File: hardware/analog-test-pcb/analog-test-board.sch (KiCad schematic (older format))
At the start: 0 parts

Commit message: Typo.
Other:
- note added: "Requirement:\nThe input to the HX1 module needs a swing from 0 to 5V\nin order to achive the ±5kHz deviation (typical specs\nfrom the datasheet).\n\nProblem:\nThe output of the DS8500 is 500mVpp (typ) with a 1.5V\nof DC offset. The maximum load at the ouput is 30kOHM\n(by specs in the datasheet). This needs to be analogly\nprocessed in order to fit the signal level required by the\nHX1 module\n\n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"
- note removed: "Requirement:\nThe input to the HX1 module need a swing from 0 to 5V\nin order to achive the ±5kHz deviation (typical specs\nfrom the datasheet).\n\nProblem:\nThe output of the DS8500 is 500mVpp (typ) with a 1.5V\nof DC offset. The maximum load at the ouput is 30kOHM\n(by specs in the datasheet). This needs to be analogly\nprocessed in order to fit the signal level required by the\nHX1 module\n\nS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"
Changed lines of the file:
@@
 $EndDescr
 Text Notes 650  2000 0    60   ~ 12
-Requirement:\nThe input to the HX1 module need a swing from 0 to 5V\nin order to achive the ±5kHz deviation (typical specs\nfrom the datasheet).\n\nProblem:\nThe output of the DS8500 is 500mVpp (typ) with a 1.5V\nof DC offset. The maximum load at the ouput is 30kOHM\n(by specs in the datasheet). This needs to be analogly\nprocessed in order to fit the signal level required by the\nHX1 module\n\nSolution:\nDo some analog processing!
+Requirement:\nThe input to the HX1 module needs a swing from 0 to 5V\nin order to achive the ±5kHz deviation (typical specs\nfrom the datasheet).\n\nProblem:\nThe output of the DS8500 is 500mVpp (typ) with a 1.5V\nof DC offset. The maximum load at the ouput is 30kOHM\n(by specs in the datasheet). This needs to be analogly\nprocessed in order to fit the signal level required by the\nHX1 module\n\nSolution:\nDo some analog processing!
 $EndSCHEMATC

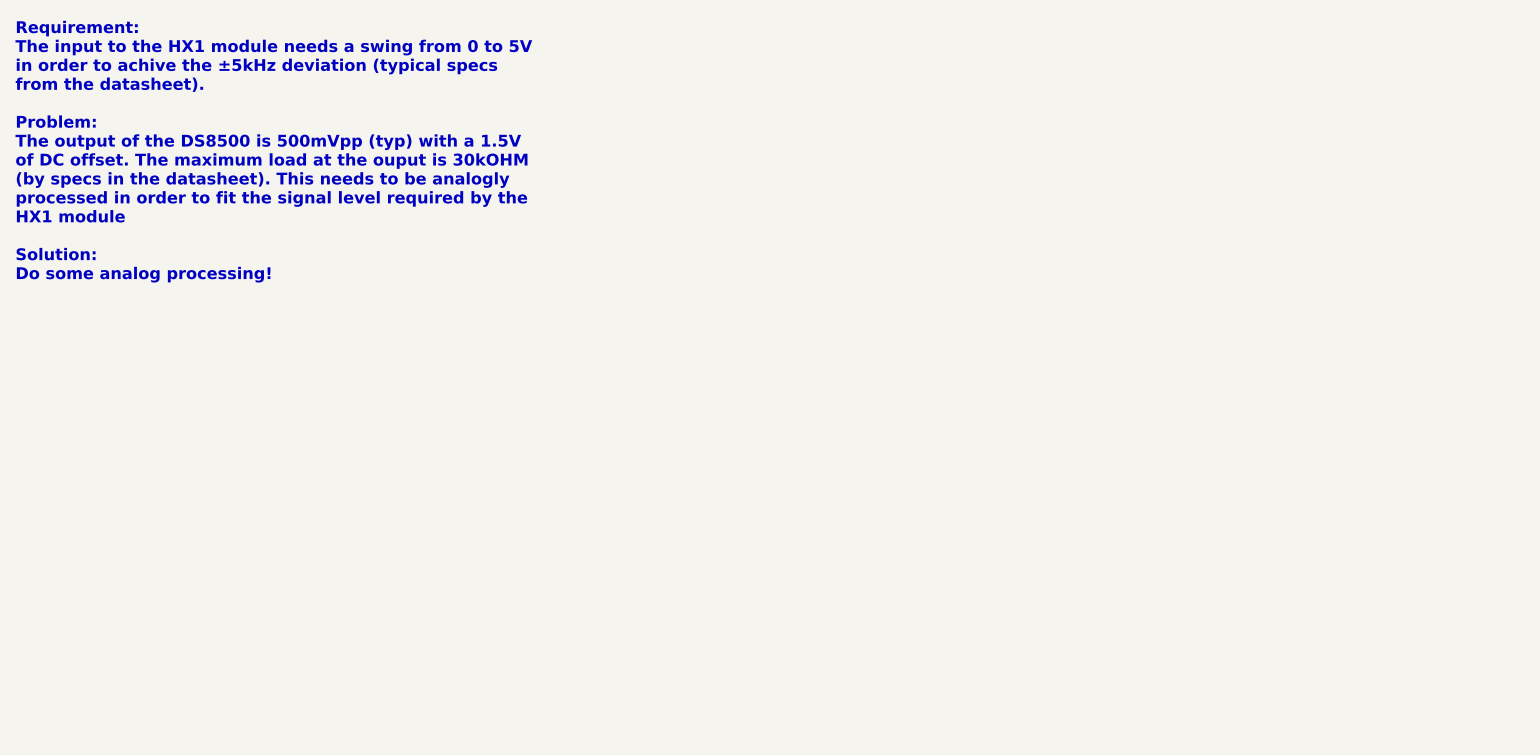
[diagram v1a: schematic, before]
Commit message: The schematic. A buffer followed by a inverting amp with a DC offset
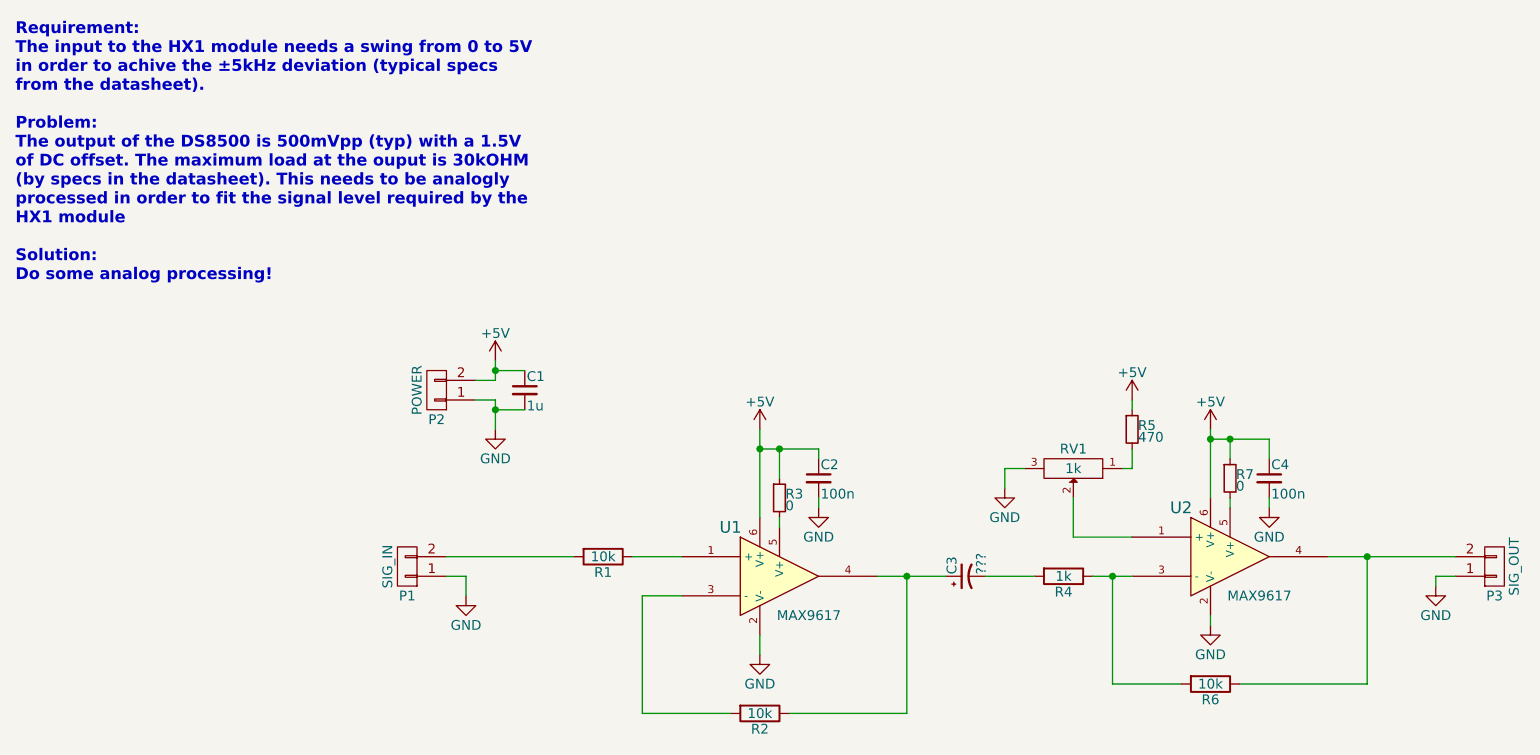
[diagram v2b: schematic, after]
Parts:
- added C1: 1u, symbol C_Small
- added C2, C4: 100n, symbol C_Small
- added C3: ???, symbol CP1_Small
- added P1: SIG_IN, symbol CONN_01X02
- added P2: POWER, symbol CONN_01X02
- added P3: SIG_OUT, symbol CONN_01X02
- added R1, R2, R6: 10k, symbol R
- added R3, R7: 0, symbol R_Small
- added R4: 1k, symbol R
- added R5: 470, symbol R_Small
- added RV1: 1k, symbol POT
- added U1, U2: MAX9617, symbol MAX9617
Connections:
- new net: R1.1, U1.1 (+)
- new net: R2.2, U1.3 (-)
- new net: C3.1, R2.1, U1.4
- new net: R3.2, U1.5 (V+)
- new net: P1.2 (P2), R1.2
- new net: C3.2, R4.2
- new net: RV1.2, U2.1 (+)
- new net: R4.1, R6.2, U2.3 (-)
- new net: P3.2 (P2), R6.1, U2.4
- new net: R7.2, U2.5 (V+)
- new net: R5.2, RV1.1
- new net +5V: C1.1, C2.1, C4.1, P2.2 (P2), R3.1, R5.1, R7.1, U1.6 (V+), U2.6 (V+)
- new net GND: C1.2, C2.2, C4.2, P1.1 (P1), P2.1 (P1), P3.1 (P1), RV1.3, U1.2 (V-), U2.2 (V-)

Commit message: First version of the pcb
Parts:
- C1: footprint (none) -> w_smd_cap:c_1206
- C2, C4: footprint (none) -> w_smd_cap:c_0805
- C3: value ??? -> >1u; footprint (none) -> w_smd_cap:c_1206
- P1, P2, P3: footprint (none) -> Pin_Headers:Pin_Header_Straight_1x02
- R1, R2, R3, R4, R5, R6, R7: footprint (none) -> w_smd_resistors:r_0805
- RV1: footprint (none) -> Potentiometer_RevB_02Aug2010:Potentiometer_Bourns_3296W_3-8Zoll_Inline_ScrewUp
- U1, U2: footprint (none) -> w_smd_trans:sc70-6
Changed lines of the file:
@@
 F 0 "U1" H 4300 3750 60  0000 C CNN
 F 1 "MAX9617" H 4700 3300 50  0000 C CNN
-F 2 "" H 4550 3500 60  0000 C CNN
+F 2 "w_smd_trans:sc70-6" H 4550 3500 60  0001 C CNN
 F 3 "" H 4550 3500 60  0000 C CNN
 	1    4550 3500
@@
 F 0 "R3" H 4580 3120 50  0000 L CNN
 F 1 "0" H 4580 3060 50  0000 L CNN
-F 2 "" H 4550 3100 50  0000 C CNN
+F 2 "w_smd_resistors:r_0805" H 4550 3100 50  0001 C CNN
 F 3 "" H 4550 3100 50  0000 C CNN
 	1    4550 3100
@@
 	4550 3200 4550 3250
 $Comp
-L GND #PWR5
+L GND #PWR01
 U 1 1 572F452A
 P 4450 3900
-F 0 "#PWR5" H 4450 3650 50  0001 C CNN
+F 0 "#PWR01" H 4450 3650 50  0001 C CNN
 F 1 "GND" H 4450 3750 50  0000 C CNN
 F 2 "" H 4450 3900 50  0000 C CNN
@@
 F 0 "R1" V 3730 3400 50  0000 C CNN
 F 1 "10k" V 3650 3400 50  0000 C CNN
-F 2 "" V 3580 3400 50  0000 C CNN
+F 2 "w_smd_resistors:r_0805" V 3580 3400 50  0001 C CNN
 F 3 "" H 3650 3400 50  0000 C CNN
 	1    3650 3400
@@
 F 0 "R2" V 4530 4200 50  0000 C CNN
 F 1 "10k" V 4450 4200 50  0000 C CNN
-F 2 "" V 4380 4200 50  0000 C CNN
+F 2 "w_smd_resistors:r_0805" V 4380 4200 50  0001 C CNN
 F 3 "" H 4450 4200 50  0000 C CNN
 	1    4450 4200
@@
 F 0 "P2" H 2800 2700 50  0000 C CNN
 F 1 "POWER" V 2900 2550 50  0000 C CNN
-F 2 "" H 2800 2550 50  0000 C CNN
+F 2 "Pin_Headers:Pin_Header_Straight_1x02" H 2800 2550 50  0001 C CNN
 F 3 "" H 2800 2550 50  0000 C CNN
 	1    2800 2550
@@
 $EndComp
 $Comp
-L GND #PWR3
+L GND #PWR02
 U 1 1 572F4851
 P 3100 2750
-F 0 "#PWR3" H 3100 2500 50  0001 C CNN
+F 0 "#PWR02" H 3100 2500 50  0001 C CNN
 F 1 "GND" H 3100 2600 50  0000 C CNN
 F 2 "" H 3100 2750 50  0000 C CNN
@@
 	3100 2600 3000 2600
 $Comp
-L +5V #PWR2
+L +5V #PWR03
 U 1 1 572F48C4
 P 3100 2400
-F 0 "#PWR2" H 3100 2250 50  0001 C CNN
+F 0 "#PWR03" H 3100 2250 50  0001 C CNN
 F 1 "+5V" H 3100 2540 50  0000 C CNN
 F 2 "" H 3100 2400 50  0000 C CNN
@@
 F 0 "C1" H 3260 2620 50  0000 L CNN
 F 1 "1u" H 3260 2470 50  0000 L CNN
-F 2 "" H 3250 2550 50  0000 C CNN
+F 2 "w_smd_cap:c_1206" H 3250 2550 50  0001 C CNN
 F 3 "" H 3250 2550 50  0000 C CNN
 	1    3250 2550
@@
 F 0 "P1" H 2650 3600 50  0000 C CNN
 F 1 "SIG_IN" V 2750 3450 50  0000 C CNN
-F 2 "" H 2650 3450 50  0000 C CNN
+F 2 "Pin_Headers:Pin_Header_Straight_1x02" H 2650 3450 50  0001 C CNN
 F 3 "" H 2650 3450 50  0000 C CNN
 	1    2650 3450
@@
 $EndComp
 $Comp
-L GND #PWR1
+L GND #PWR04
 U 1 1 572F4ADF
 P 2950 3600
-F 0 "#PWR1" H 2950 3350 50  0001 C CNN
+F 0 "#PWR04" H 2950 3350 50  0001 C CNN
 F 1 "GND" H 2950 3450 50  0000 C CNN
 F 2 "" H 2950 3600 50  0000 C CNN
@@
 	2850 3400 3500 3400
 $Comp
-L +5V #PWR4
+L +5V #PWR05
 U 1 1 572F4C22
 P 4450 2750
-F 0 "#PWR4" H 4450 2600 50  0001 C CNN
+F 0 "#PWR05" H 4450 2600 50  0001 C CNN
 F 1 "+5V" H 4450 2890 50  0000 C CNN
 F 2 "" H 4450 2750 50  0000 C CNN
@@
 F 0 "C2" H 4760 3070 50  0000 L CNN
 F 1 "100n" H 4760 2920 50  0000 L CNN
-F 2 "" H 4750 3000 50  0000 C CNN
+F 2 "w_smd_cap:c_0805" H 4750 3000 50  0001 C CNN
 F 3 "" H 4750 3000 50  0000 C CNN
 	1    4750 3000
@@
 Connection ~ 4550 2850
 $Comp
-L GND #PWR6
+L GND #PWR06
 U 1 1 572F4CCE
 P 4750 3150
-F 0 "#PWR6" H 4750 2900 50  0001 C CNN
+F 0 "#PWR06" H 4750 2900 50  0001 C CNN
 F 1 "GND" H 4750 3000 50  0000 C CNN
 F 2 "" H 4750 3150 50  0000 C CNN
@@
 P 5500 3500
 F 0 "C3" H 5510 3570 50  0000 L CNN
-F 1 "???" H 5510 3420 50  0000 L CNN
-F 2 "" H 5500 3500 50  0000 C CNN
+F 1 ">1u" H 5510 3420 50  0000 L CNN
+F 2 "w_smd_cap:c_1206" H 5500 3500 50  0001 C CNN
 F 3 "" H 5500 3500 50  0000 C CNN
 	1    5500 3500
@@
 F 0 "U2" H 6600 3650 60  0000 C CNN
 F 1 "MAX9617" H 7000 3200 50  0000 C CNN
-F 2 "" H 6850 3400 60  0000 C CNN
+F 2 "w_smd_trans:sc70-6" H 6850 3400 60  0001 C CNN
 F 3 "" H 6850 3400 60  0000 C CNN
 	1    6850 3400
@@
 F 0 "R4" V 6080 3500 50  0000 C CNN
 F 1 "1k" V 6000 3500 50  0000 C CNN
-F 2 "" V 5930 3500 50  0000 C CNN
+F 2 "w_smd_resistors:r_0805" V 5930 3500 50  0001 C CNN
 F 3 "" H 6000 3500 50  0000 C CNN
 	1    6000 3500
@@
 	5850 3500 5600 3500
 $Comp
-L GND #PWR10
+L GND #PWR07
 U 1 1 572F5105
 P 6750 3750
-F 0 "#PWR10" H 6750 3500 50  0001 C CNN
+F 0 "#PWR07" H 6750 3500 50  0001 C CNN
 F 1 "GND" H 6750 3600 50  0000 C CNN
 F 2 "" H 6750 3750 50  0000 C CNN
@@
 F 0 "R6" V 6830 4050 50  0000 C CNN
 F 1 "10k" V 6750 4050 50  0000 C CNN
-F 2 "" V 6680 4050 50  0000 C CNN
+F 2 "w_smd_resistors:r_0805" V 6680 4050 50  0001 C CNN
 F 3 "" H 6750 4050 50  0000 C CNN
 	1    6750 4050
@@
 F 0 "P3" H 8200 3600 50  0000 C CNN
 F 1 "SIG_OUT" V 8300 3450 50  0000 C CNN
-F 2 "" H 8200 3450 50  0000 C CNN
+F 2 "Pin_Headers:Pin_Header_Straight_1x02" H 8200 3450 50  0001 C CNN
 F 3 "" H 8200 3450 50  0000 C CNN
 	1    8200 3450
@@
 Connection ~ 7550 3400
 $Comp
-L GND #PWR12
+L GND #PWR08
 U 1 1 572F538D
 P 7900 3550
-F 0 "#PWR12" H 7900 3300 50  0001 C CNN
+F 0 "#PWR08" H 7900 3300 50  0001 C CNN
 F 1 "GND" H 7900 3400 50  0000 C CNN
 F 2 "" H 7900 3550 50  0000 C CNN
@@
 F 0 "R7" H 6880 3020 50  0000 L CNN
 F 1 "0" H 6880 2960 50  0000 L CNN
-F 2 "" H 6850 3000 50  0000 C CNN
+F 2 "w_smd_resistors:r_0805" H 6850 3000 50  0001 C CNN
 F 3 "" H 6850 3000 50  0000 C CNN
 	1    6850 3000
@@
 	6750 2750 6750 3100
 $Comp
-L +5V #PWR9
+L +5V #PWR09
 U 1 1 572F5634
 P 6750 2750
-F 0 "#PWR9" H 6750 2600 50  0001 C CNN
+F 0 "#PWR09" H 6750 2600 50  0001 C CNN
 F 1 "+5V" H 6750 2890 50  0000 C CNN
 F 2 "" H 6750 2750 50  0000 C CNN
@@
 F 0 "C4" H 7060 3070 50  0000 L CNN
 F 1 "100n" H 7060 2920 50  0000 L CNN
-F 2 "" H 7050 3000 50  0000 C CNN
+F 2 "w_smd_cap:c_0805" H 7050 3000 50  0001 C CNN
 F 3 "" H 7050 3000 50  0000 C CNN
 	1    7050 3000
@@
 Connection ~ 6850 2800
 $Comp
-L GND #PWR11
+L GND #PWR010
 U 1 1 572F575F
 P 7050 3150
-F 0 "#PWR11" H 7050 2900 50  0001 C CNN
+F 0 "#PWR010" H 7050 2900 50  0001 C CNN
 F 1 "GND" H 7050 3000 50  0000 C CNN
 F 2 "" H 7050 3150 50  0000 C CNN
@@
 F 0 "RV1" H 6050 2850 50  0000 C CNN
 F 1 "1k" H 6050 2950 50  0000 C CNN
-F 2 "" H 6050 2950 50  0000 C CNN
+F 2 "Potentiometer_RevB_02Aug2010:Potentiometer_Bourns_3296W_3-8Zoll_Inline_ScrewUp" H 6050 2950 50  0001 C CNN
 F 3 "" H 6050 2950 50  0000 C CNN
 	1    6050 2950
@@
 F 0 "R5" H 6380 2770 50  0000 L CNN
 F 1 "470" H 6380 2710 50  0000 L CNN
-F 2 "" H 6350 2750 50  0000 C CNN
+F 2 "w_smd_resistors:r_0805" H 6350 2750 50  0001 C CNN
 F 3 "" H 6350 2750 50  0000 C CNN
 	1    6350 2750
@@
 	6050 3300 6350 3300
 $Comp
-L GND #PWR7
+L GND #PWR011
 U 1 1 572F5A83
 P 5700 3050
-F 0 "#PWR7" H 5700 2800 50  0001 C CNN
+F 0 "#PWR011" H 5700 2800 50  0001 C CNN
 F 1 "GND" H 5700 2900 50  0000 C CNN
 F 2 "" H 5700 3050 50  0000 C CNN
@@
 	5700 2950 5800 2950
 $Comp
-L +5V #PWR8
+L +5V #PWR012
 U 1 1 572F5BE9
 P 6350 2600
-F 0 "#PWR8" H 6350 2450 50  0001 C CNN
+F 0 "#PWR012" H 6350 2450 50  0001 C CNN
 F 1 "+5V" H 6350 2740 50  0000 C CNN
 F 2 "" H 6350 2600 50  0000 C CNN
